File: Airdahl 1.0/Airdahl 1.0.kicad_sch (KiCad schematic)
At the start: 47 parts, among them J1 Conn_01x04, J2 DF40C-34DS-0.4V_58_, J3 DF40C-34DS-0.4V_58_, J4 USB_C_Receptacle_USB2.0_16P, SW1 SW_MEC_5E, SW2 SW_MEC_5E, U1 STM32F446RETx, U2 MCP2200-I-MQ, U3 LT1963AxST-3.3, Y1 ABM3B-8.000MHZ-12-D1X-T, Y2 ABS25-32.768KHZ-6-T, Y3 12MHz

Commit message: apparently you can use mlcc with the ldo oop
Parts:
- removed C1, C2: 10u TANT, Capacitor_SMD:C_1206_3216Metric, symbol Device:C_Polarized_US
- added C1, C2: 10u, Capacitor_SMD:C_0805_2012Metric, symbol Device:C
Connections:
- net GND: now also C1.2, C2.2
- net USB_3V3: now also C2.1
- net VBUS: now also C1.1
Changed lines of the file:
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@@
 	)
 	(junction
+		(at 110.49 77.47)
+		(diameter 0)
+		(color 0 0 0 0)
+	)
+	(junction
 		(at 207.01 214.63)
 		(diameter 0)
@@
 	)
 	(junction
-		(at 139.7 77.47)
-		(diameter 0)
-		(color 0 0 0 0)
-	)
-	(junction
 		(at 245.11 91.44)
 		(diameter 0)
@@
 	)
 	(junction
-		(at 311.15 83.82)
+		(at 139.7 77.47)
 		(diameter 0)
 		(color 0 0 0 0)
 	)
 	(junction
-		(at 110.49 77.47)
+		(at 311.15 83.82)
 		(diameter 0)
 		(color 0 0 0 0)
@@
 	(wire
 		(pts
+			(xy 110.49 77.47) (xy 114.3 77.47)
+		)
+		(stroke
+			(width 0)
+			(type default)
+		)
+	)
+	(wire
+		(pts
 			(xy 278.13 82.55) (xy 278.13 83.82)
 		)
@@
 	(wire
 		(pts
-			(xy 110.49 77.47) (xy 114.3 77.47)
+			(xy 88.9 77.47) (xy 110.49 77.47)
 		)
 		(stroke
@@
 	(wire
 		(pts
-			(xy 88.9 77.47) (xy 110.49 77.47)
-		)
-		(stroke
-			(width 0)
-			(type default)
-		)
-	)
-	(wire
-		(pts
 			(xy 166.37 110.49) (xy 166.37 111.76)
 		)
@@
 	)
 	(symbol
-		(lib_id "Device:C_Polarized_US")
+		(lib_id "Device:C")
 		(at 139.7 81.28 0)
 		(unit 1)
@@
 		(dnp no)
 		(property "Reference" "C2"
-			(at 143.51 79.3749 0)
+			(at 143.51 80.0099 0)
 			(show_name no)
 			(do_not_autoplace no)
@@
 			)
 		)
-		(property "Value" "10u TANT"
-			(at 143.51 81.9149 0)
+		(property "Value" "10u"
+			(at 143.51 82.5499 0)
 			(show_name no)
 			(do_not_autoplace no)
@@
 			)
 		)
-		(property "Footprint" "Capacitor_SMD:C_1206_3216Metric"
-			(at 139.7 81.28 0)
+		(property "Footprint" "Capacitor_SMD:C_0805_2012Metric"
+			(at 140.6652 85.09 0)
 			(hide yes)
 			(show_name no)
@@
 			)
 		)
-		(property "Description" "Polarized capacitor, US symbol"
+		(property "Description" "Unpolarized capacitor"
 			(at 139.7 81.28 0)
 			(hide yes)
@@
 	)
 	(symbol
+		(lib_id "Device:C")
+		(at 110.49 81.28 0)
+		(mirror y)
+		(unit 1)
+		(body_style 1)
+		(exclude_from_sim no)
+		(in_bom yes)
+		(on_board yes)
+		(in_pos_files yes)
+		(dnp no)
+		(property "Reference" "C1"
+			(at 106.68 80.0099 0)
+			(show_name no)
+			(do_not_autoplace no)
+			(effects
+				(font
+					(size 1.27 1.27)
+				)
+				(justify left)
+			)
+		)
+		(property "Value" "10u"
+			(at 106.68 82.5499 0)
+			(show_name no)
+			(do_not_autoplace no)
+			(effects
+				(font
+					(size 1.27 1.27)
+				)
+				(justify left)
+			)
+		)
+		(property "Footprint" "Capacitor_SMD:C_0805_2012Metric"
+			(at 109.5248 85.09 0)
+			(hide yes)
+			(show_name no)
+			(do_not_autoplace no)
+			(effects
+				(font
+					(size 1.27 1.27)
+				)
+			)
+		)
+		(property "Datasheet" ""
+			(at 110.49 81.28 0)
+			(hide yes)
+			(show_name no)
+			(do_not_autoplace no)
+			(effects
+				(font
+					(size 1.27 1.27)
+				)
+			)
+		)
+		(property "Description" "Unpolarized capacitor"
+			(at 110.49 81.28 0)
+			(hide yes)
+			(show_name no)
+			(do_not_autoplace no)
+			(effects
+				(font
+					(size 1.27 1.27)
+				)
+			)
+		)
+		(pin "2"
+		)
+		(pin "1"
+		)
+		(instances
+			(project "Airdahl 1.0"
+				(path "/e2c992a5-0f37-48ff-88a4-7c40cfcda45e"
+					(reference "C1")
+					(unit 1)
+				)
+			)
+		)
+	)
+	(symbol
 		(lib_id "power:+3V3")
 		(at 114.3 44.45 0)
@@
 					(unit 1)
 				)
-			)
-		)
-	)
-	(symbol
-		(lib_id "Device:C_Polarized_US")
-		(at 110.49 81.28 0)
-		(mirror y)
-		(unit 1)
-		(body_style 1)
-		(exclude_from_sim no)
-		(in_bom yes)
-		(on_board yes)
-		(in_pos_files yes)
-		(dnp no)
-		(property "Reference" "C1"
-			(at 106.68 79.3749 0)
-			(show_name no)
-			(do_not_autoplace no)
-			(effects
-				(font
-					(size 1.27 1.27)
-				)
-				(justify left)
-			)
-		)
-		(property "Value" "10u TANT"
-			(at 106.68 81.9149 0)
-			(show_name no)
-			(do_not_autoplace no)
-			(effects
-				(font
-					(size 1.27 1.27)
-				)
-				(justify left)
-			)
-		)
-		(property "Footprint" "Capacitor_SMD:C_1206_3216Metric"
-			(at 110.49 81.28 0)
-			(hide yes)
-			(show_name no)
-			(do_not_autoplace no)
-			(effects
-				(font
-					(size 1.27 1.27)
-				)
-			)
-		)
-		(property "Datasheet" ""
-			(at 110.49 81.28 0)
-			(hide yes)
-			(show_name no)
-			(do_not_autoplace no)
-			(effects
-				(font
-					(size 1.27 1.27)
-				)
-			)
-		)
-		(property "Description" "Polarized capacitor, US symbol"
-			(at 110.49 81.28 0)
-			(hide yes)
-			(show_name no)
-			(do_not_autoplace no)
-			(effects
-				(font
-					(size 1.27 1.27)
-				)
-			)
-		)
-		(pin "2"
-		)
-		(pin "1"
-		)
-		(instances
-			(project "Airdahl 1.0"
-				(path "/e2c992a5-0f37-48ff-88a4-7c40cfcda45e"
-					(reference "C1")
-					(unit 1)
-				)

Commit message: added led and others
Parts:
- removed C38: 470n, Capacitor_SMD:C_0603_1608Metric_Pad1.08x0.95mm_HandSolder, symbol Device:C_Small
- added BT1: Battery_Cell, Battery:BatteryHolder_Keystone_1060_1x2032, symbol Device:Battery_Cell
- added C16: 100n, Capacitor_SMD:C_0603_1608Metric_Pad1.08x0.95mm_HandSolder, symbol Device:C_Small
- added D2, D3: LEDY, LED_SMD:LED_0603_1608Metric, symbol Device:LED
- added D4: LEDG, LED_SMD:LED_0603_1608Metric, symbol Device:LED
- added D5: LEDR, LED_SMD:LED_0603_1608Metric, symbol Device:LED
- added R45: 470, Resistor_SMD:R_0402_1005Metric, symbol Device:R_Small
- added R46: 10k, Resistor_SMD:R_0402_1005Metric, symbol Device:R_Small
- added R47: 22, Resistor_SMD:R_0402_1005Metric, symbol Device:R_Small
- added R48, R49, R50, R51: 500, Resistor_SMD:R_0402_1005Metric, symbol Device:R_Small
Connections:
- net +3V3: now also C37.1, SW2.1, SW2.2, U2.14 (V_USB), U2.18 (VDD), R46.2, R48.2, R49.2, R50.2; no longer C15.1, C29.1, SW2.3 (K), SW2.4 (A), U1.1 (VBAT)
- net BOOT0: now also SW2.3 (K), SW2.4 (A); no longer SW2.1, SW2.2
- net CS_RFM: no longer U1.20 (PA4)
- net GND: now also C15.1, BT1.2 (-), C16.1, D4.1 (K), D5.1 (K)
- net MOSI: no longer U1.23 (PA7)
- net SCLK: no longer U1.21 (PA5)
- net USB_3V3: no longer C37.1, U2.18 (VDD)
- net MCP_RST: now reaches U2.1 (~{RST})
- net MCP_RST: now also R45.1
- net at U2.2 (GP7/TxLED): now also D3.1 (K)
- net at U2.3 (GP6/RxLED): now also D2.1 (K)
- net at U1.50 (PA15): now also R47.2
- net Primary Sensors/CS_RFM: no longer names the net of R40.2
- net Primary Sensors/CS_RFM: now also U1.20 (PA4)
- net Primary Sensors/MOSI: no longer names the net of R42.2
- net Primary Sensors/MOSI: now also U1.23 (PA7)
- net Primary Sensors/SCLK: no longer names the net of R41.2
- net Primary Sensors/SCLK: now also U1.21 (PA5)
- net SWO: no longer names the net of U1.55 (PB3)
- new net: D2.2 (A), R48.1
- new net: C16.2, R45.2, R46.1
- new net: D4.2 (A), R50.1
- new net: D3.2 (A), R49.1
- new net: D5.2 (A), R51.1
- new net CS_SD: R47.1
- new net DEBUG_LED: R51.2
- new net VBAT: BT1.1 (+), C29.1, U1.1 (VBAT)
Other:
- sheet Primary Sensors ports: added CS_SD; removed none
- note added: "Power Supply OR-ing"
- note added: "RTC Battery"
- note added: "UART-to-USB Interface"
- note added: "VBUS LDO"
- note removed: "UART Interface"
- moved on the sheet: R17, R18, R40, R41, R42, SW1

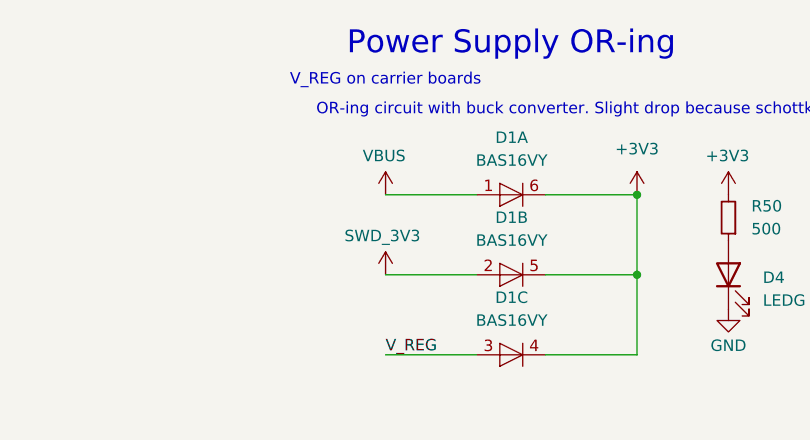
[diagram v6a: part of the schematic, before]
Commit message: vbus is no longer shorted to 3v3
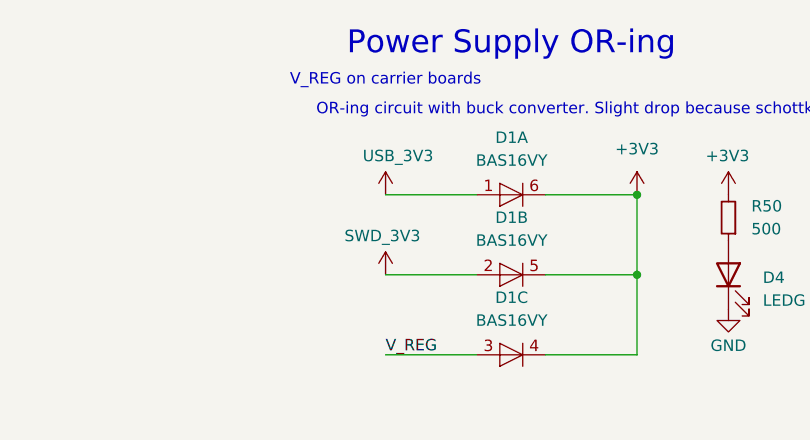
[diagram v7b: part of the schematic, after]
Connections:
- net USB_3V3: now also D1.1 (A)
- net VBUS: no longer D1.1 (A)
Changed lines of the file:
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@@
 			)
 		)
-		(property "Value" "VBUS"
+		(property "Value" "USB_3V3"
 			(at 111.76 31.242 0)
 			(show_name no)
